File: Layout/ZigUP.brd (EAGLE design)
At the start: 53 x 47 mm, 36 parts, among them IC1 IRM-02-3.3, IC2 CC2530, K1 DSP2A-L2-DC3V, T1 IRFML8244, T2 IRFML8244, X1 Phoenix 1792876, X2 TE 1-2834021-4, X3 TE 1-2834021-4, X4 DEBUG

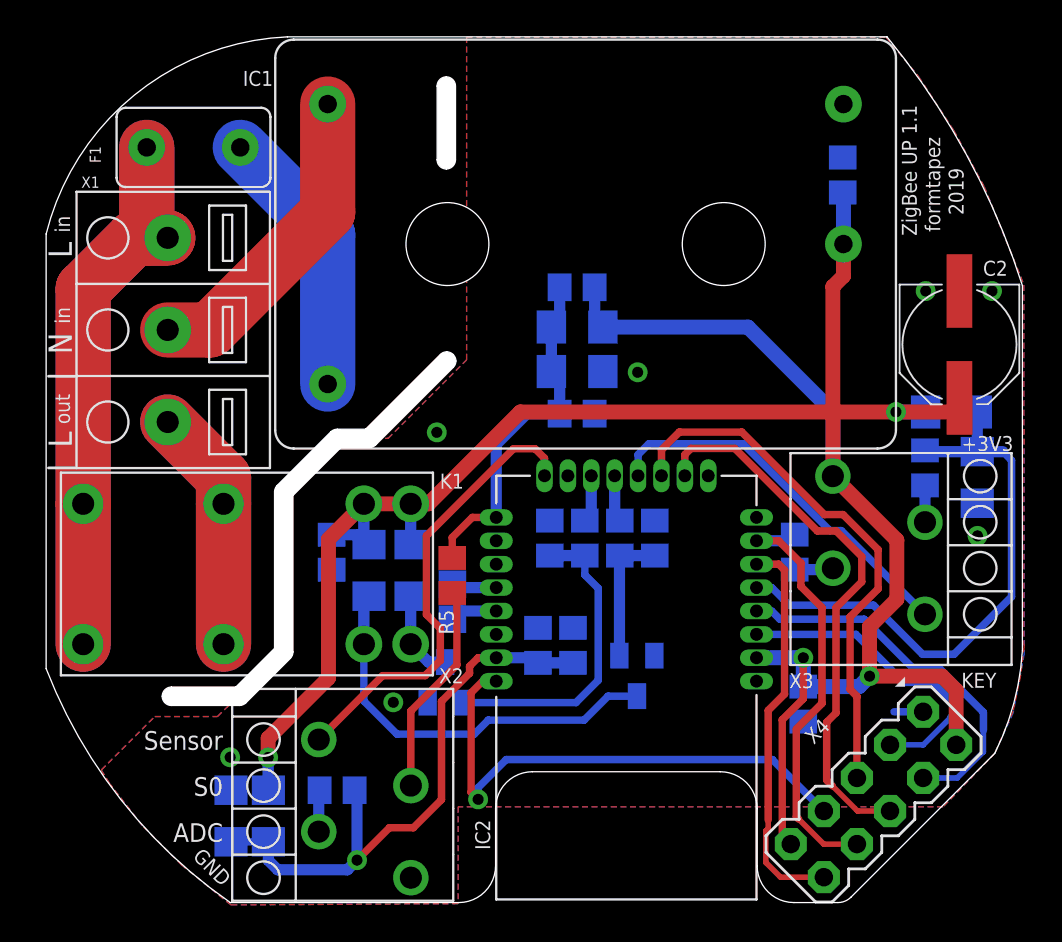
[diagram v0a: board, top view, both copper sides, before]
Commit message: Added accelerometer MMA845x
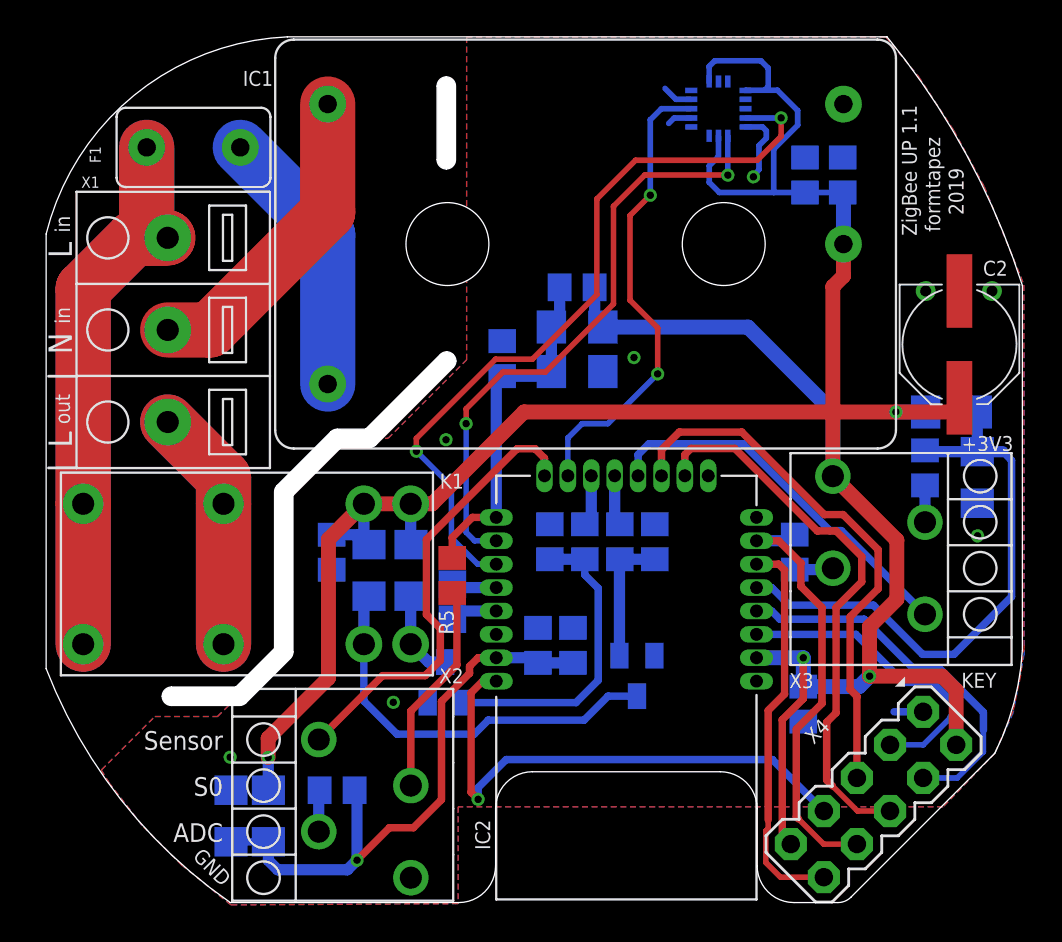
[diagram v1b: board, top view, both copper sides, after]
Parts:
- added C7: 4.7µ, rcl:C0805
- added U1: MMA8452QT, mma8452:QFN50P300X300X100-16N
- moved C4 5.05 mm to (24.8, 29.5), turned to 90 degrees
- moved R1 0.20 mm to (29.2, 19.6)
- moved R2 0.20 mm to (27.3, 19.6)
- moved R3 0.20 mm to (31.1, 19.6)
- moved R4 0.20 mm to (33.0, 19.6)
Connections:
- new net ACC_INT: IC2.15, U1.11
- new net ACC_SCL: IC2.19, U1.4
- new net ACC_SDA: IC2.18, U1.6
- net +3V3: now also C7.2, U1.1, U1.14, U1.7
- net GND: now also C7.1, U1.10, U1.12, U1.5
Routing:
- net ACC_SCL: track 0.00 -> 42.0 mm, vias 0 -> 2
- net ACC_SDA: track 0.00 -> 33.4 mm, vias 0 -> 2
- net ACC_INT: track 0.00 -> 25.7 mm, vias 0 -> 2
- net +3V3: track 136.5 -> 160.6 mm
- net GND: track 1.58 -> 8.80 mm, vias 7 -> 8
- net !S0: track 19.3 -> 19.9 mm

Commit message: final release version
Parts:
- added C8, C9: 100n, rcl:C0805
- added LED1: RED, led:LED3MM
- added LED2: (no value), led:SML0805
- added R11, R12, R13: 10k, rcl:R0805
- added R14: (no value), rcl:R0805
- C2: device rcl:PANASONIC_D -> rcl:E2,5-6
- moved C1 7.67 mm to (41.4, 32.1), turned to 180 degrees
- moved C7 5.66 mm to (40.4, 45.1), turned to 0 degrees
- moved U1 1.00 mm to (35.5, 43.1)
- moved C3 0.30 mm to (15.2, 19.0)
- moved R6 0.30 mm to (28.8, 33.7)
- moved C2 0.26 mm to (49.4, 30.5), turned to 90 degrees
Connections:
- new net LED: IC2.22, R13.2
- new net N$1: C9.2, U1.2
- new net N$2: LED1.A, R13.1
- new net N$9: LED2.A, R14.2
- net +3V3: now also C8.2, R11.2, R12.2, R14.1
- net ACC_SCL: now also R11.1
- net ACC_SDA: now also R12.1
- net GND: now also C8.1, C9.1, LED1.K, LED2.C
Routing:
- net LED: track 0.00 -> 42.0 mm, vias 0 -> 3
- net +3V3: track 160.6 -> 183.6 mm, vias 4 -> 5
- net GND: track 8.80 -> 21.5 mm, vias 8 -> 9
- net ACC_INT: track 25.7 -> 34.9 mm
- net N$1: track 0.00 -> 8.50 mm
- net N$9: track 0.00 -> 7.20 mm, vias 0 -> 1
- net ACC_SDA: track 33.4 -> 38.2 mm
- net N$2: track 0.00 -> 3.84 mm
- net ACC_SCL: track 42.0 -> 44.3 mm, vias 2 -> 3
- net !S0: track 19.9 -> 20.8 mm
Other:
- board text added: "ZigBeeUp"
- board text removed: "2019"
- board text removed: "ZigBee UP 1.1"
- board text removed: "formtapez"
